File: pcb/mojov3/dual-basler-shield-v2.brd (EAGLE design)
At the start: 78.7 x 63.5 mm, 6 parts, among them Y1 SI514

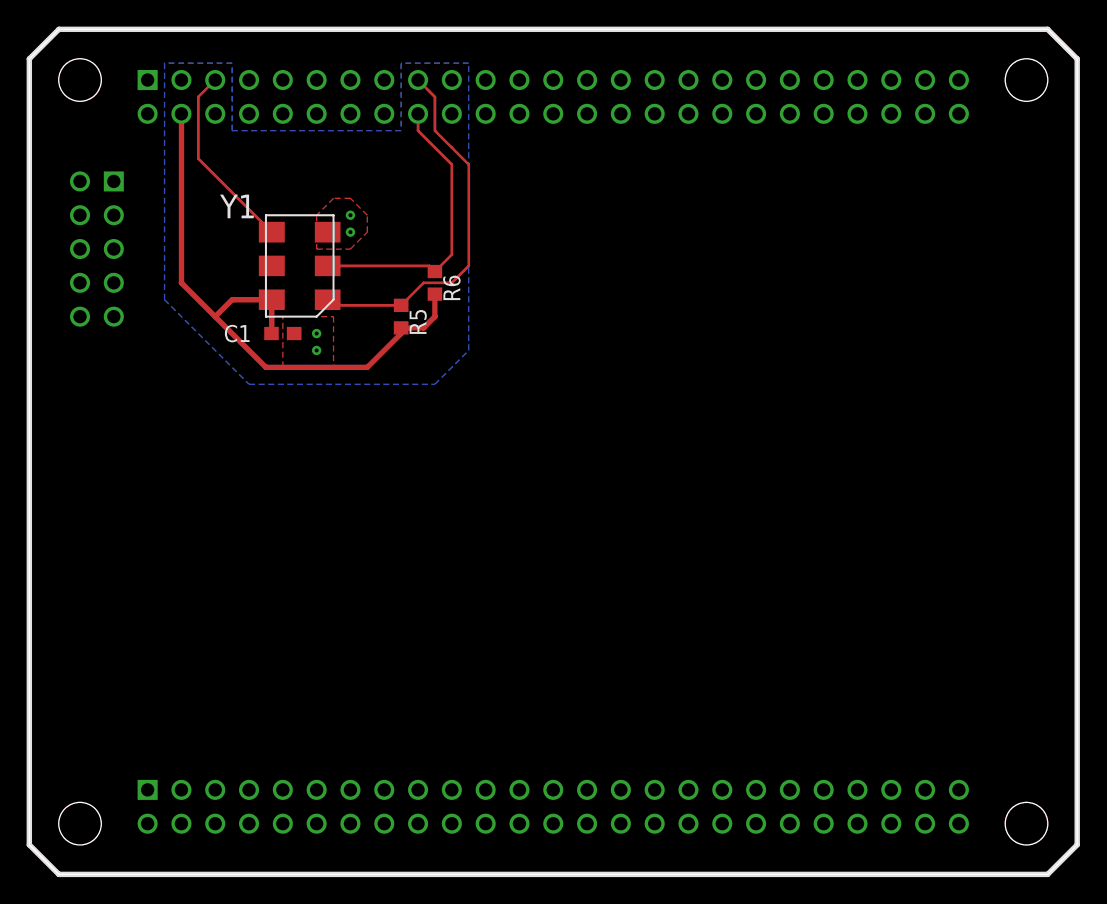
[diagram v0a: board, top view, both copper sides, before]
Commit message: routed new mojo board
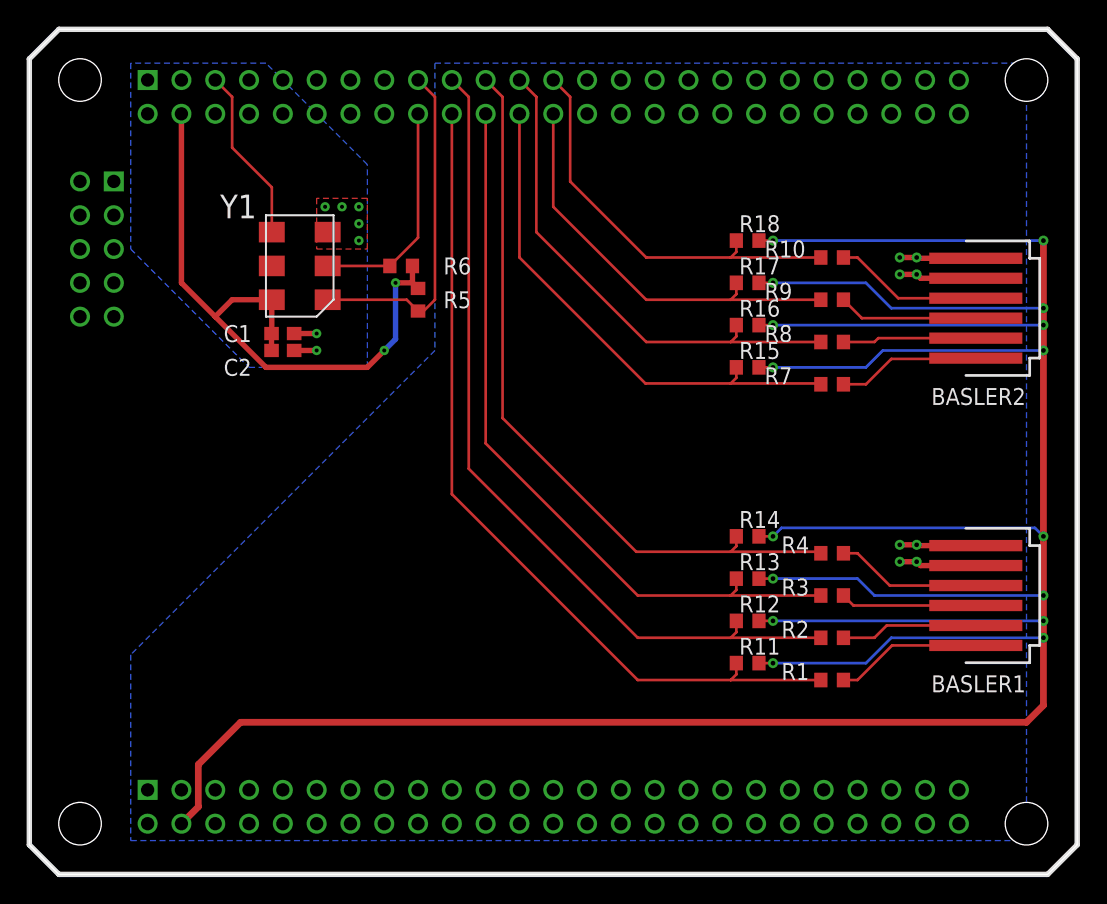
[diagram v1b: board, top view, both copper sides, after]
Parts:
- added BASLER1, BASLER2: 87438-06, con-molex:87438-06
- added C2: 1uF, rcl:C0603
- added R1, R10, R11, R12, R13, R14, R15, R16, R17, R18, R2, R3, R4, R7, R8, R9: (no value), resistor:R0603
- moved R6 2.84 mm to (27.9, 45.7), turned to 0 degrees
- moved R5 1.80 mm to (29.2, 43.2), turned to 90 degrees
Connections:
- new net N$1: BASLER1.1, R1.2
- new net N$2: BASLER1.2, R2.2
- new net N$3: BASLER1.3, R3.2
- new net N$4: BASLER1.4, R4.2
- new net N$5: BASLER2.1, R7.2
- new net N$6: BASLER2.2, R8.2
- new net N$7: BASLER2.3, R9.2
- new net N$8: BASLER2.4, R10.2
- net 3V3: now also R11.2, R12.2, R13.2, R14.2, R15.2, R16.2, R17.2, R18.2
- net GND: now also BASLER1.5, BASLER1.6, BASLER2.5, BASLER2.6, C2.2
- net LINE_1_1: now also R14.1, R4.1
- net LINE_1_2: now also R13.1, R3.1
- net LINE_1_3: now also R12.1, R2.1
- net LINE_1_4: now also R1.1, R11.1
- net LINE_2_1: now also R10.1, R18.1
- net LINE_2_2: now also R17.1, R9.1
- net LINE_2_3: now also R16.1, R8.1
- net LINE_2_4: now also R15.1, R7.1
- net VDD: now also C2.1
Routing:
- net 3V3: track 0.00 -> 279.4 mm, vias 0 -> 16
- net LINE_1_4: track 0.00 -> 63.5 mm
- net LINE_1_3: track 0.00 -> 62.9 mm
- net LINE_1_2: track 0.00 -> 56.1 mm
- net LINE_1_1: track 0.00 -> 55.4 mm
- net LINE_2_4: track 0.00 -> 38.8 mm
- net LINE_2_3: track 0.00 -> 38.2 mm
- net LINE_2_2: track 0.00 -> 31.4 mm
- net LINE_2_1: track 0.00 -> 30.8 mm
- net GND: track 0.00 -> 26.5 mm, vias 4 -> 15
- net N$8: track 0.00 -> 11.2 mm
- net N$1: track 0.00 -> 11.0 mm
- net N$4: track 0.00 -> 10.9 mm
- net N$5: track 0.00 -> 10.8 mm
- net N$7: track 0.00 -> 10.5 mm
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
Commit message: finished basler shield v2
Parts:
- added LINE_1_1, LINE_1_2, LINE_1_3, LINE_1_4, LINE_2_1, LINE_2_2, LINE_2_3, LINE_2_4, TP_GND: TPTP16R, testpad:TP16R
- added R19, R20, R21, R22, R23, R24, R25, R26: (no value), rcl:R0603
- R1, R10, R11, R12, R13, R14, R15, R16, R17, R18, R2, R3, R4, R7, R8, R9: device resistor:R0603 -> rcl:R0603
- moved R5 3.24 mm to (29.8, 46.4), turned to 270 degrees
- moved R14 2.69 mm to (56.7, 25.4)
- moved R17 2.68 mm to (56.6, 44.8)
- moved R13 2.68 mm to (56.6, 22.5)
- moved R16 2.66 mm to (56.6, 41.6)
- moved R18 2.64 mm to (56.6, 47.6)
- moved R12 2.62 mm to (56.6, 19.3)
- moved R15 2.60 mm to (56.6, 38.4)
- moved R11 2.56 mm to (56.5, 16.2)
- moved R6 0.90 mm to (27.3, 46.4), turned to 270 degrees
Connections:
- net GND: now also R19.1, R20.1, R21.1, R22.1, R23.1, R24.1, R25.1, R26.1, TP_GND.TP
- net LINE_1_1: now also LINE_1_1.TP, R22.2
- net LINE_1_2: now also LINE_1_2.TP, R21.2
- net LINE_1_3: now also LINE_1_3.TP, R20.2
- net LINE_1_4: now also LINE_1_4.TP, R19.2
- net LINE_2_1: now also LINE_2_1.TP, R26.2
- net LINE_2_2: now also LINE_2_2.TP, R25.2
- net LINE_2_3: now also LINE_2_3.TP, R24.2
- net LINE_2_4: now also LINE_2_4.TP, R23.2
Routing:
- net GND: track 26.5 -> 78.3 mm, vias 15 -> 23
- net 3V3: track 279.4 -> 258.6 mm
- net VDD: track 48.3 -> 52.5 mm, vias 2 -> 3
- net LINE_2_2: track 31.4 -> 34.4 mm
- net LINE_2_3: track 38.2 -> 41.0 mm
- net LINE_1_4: track 63.5 -> 66.3 mm
- net LINE_1_2: track 56.1 -> 58.9 mm
- net LINE_2_4: track 38.8 -> 41.5 mm
- net LINE_1_3: track 62.9 -> 65.6 mm
- net LINE_1_1: track 55.4 -> 57.9 mm
- net LINE_2_1: track 30.8 -> 33.3 mm
- net SDA: track 26.4 -> 24.4 mm
- net SCL: track 17.0 -> 16.2 mm
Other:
- board text added: "Camera 1 Config"
- board text added: "Camera 2 Config"
- board text added: "GND"
- board text added: "MojoV3 Basler Interface Dr. Daniel L. Lau Matt Ruffner Ying Yu University of Kentucky 2019"
- board text added: "Programmable Oscillator"
- board text added: "Pull Down"
- board text added: "Pull Up"
- board text added: "Series"
